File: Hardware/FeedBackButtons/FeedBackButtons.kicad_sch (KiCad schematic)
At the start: 15 parts, among them J1 Barrel_Jack_MountingPin, J2 RJ45, U1 ESP8266-01{slash}ESP-01, U2 AMS1117-3.3, U3 4N25

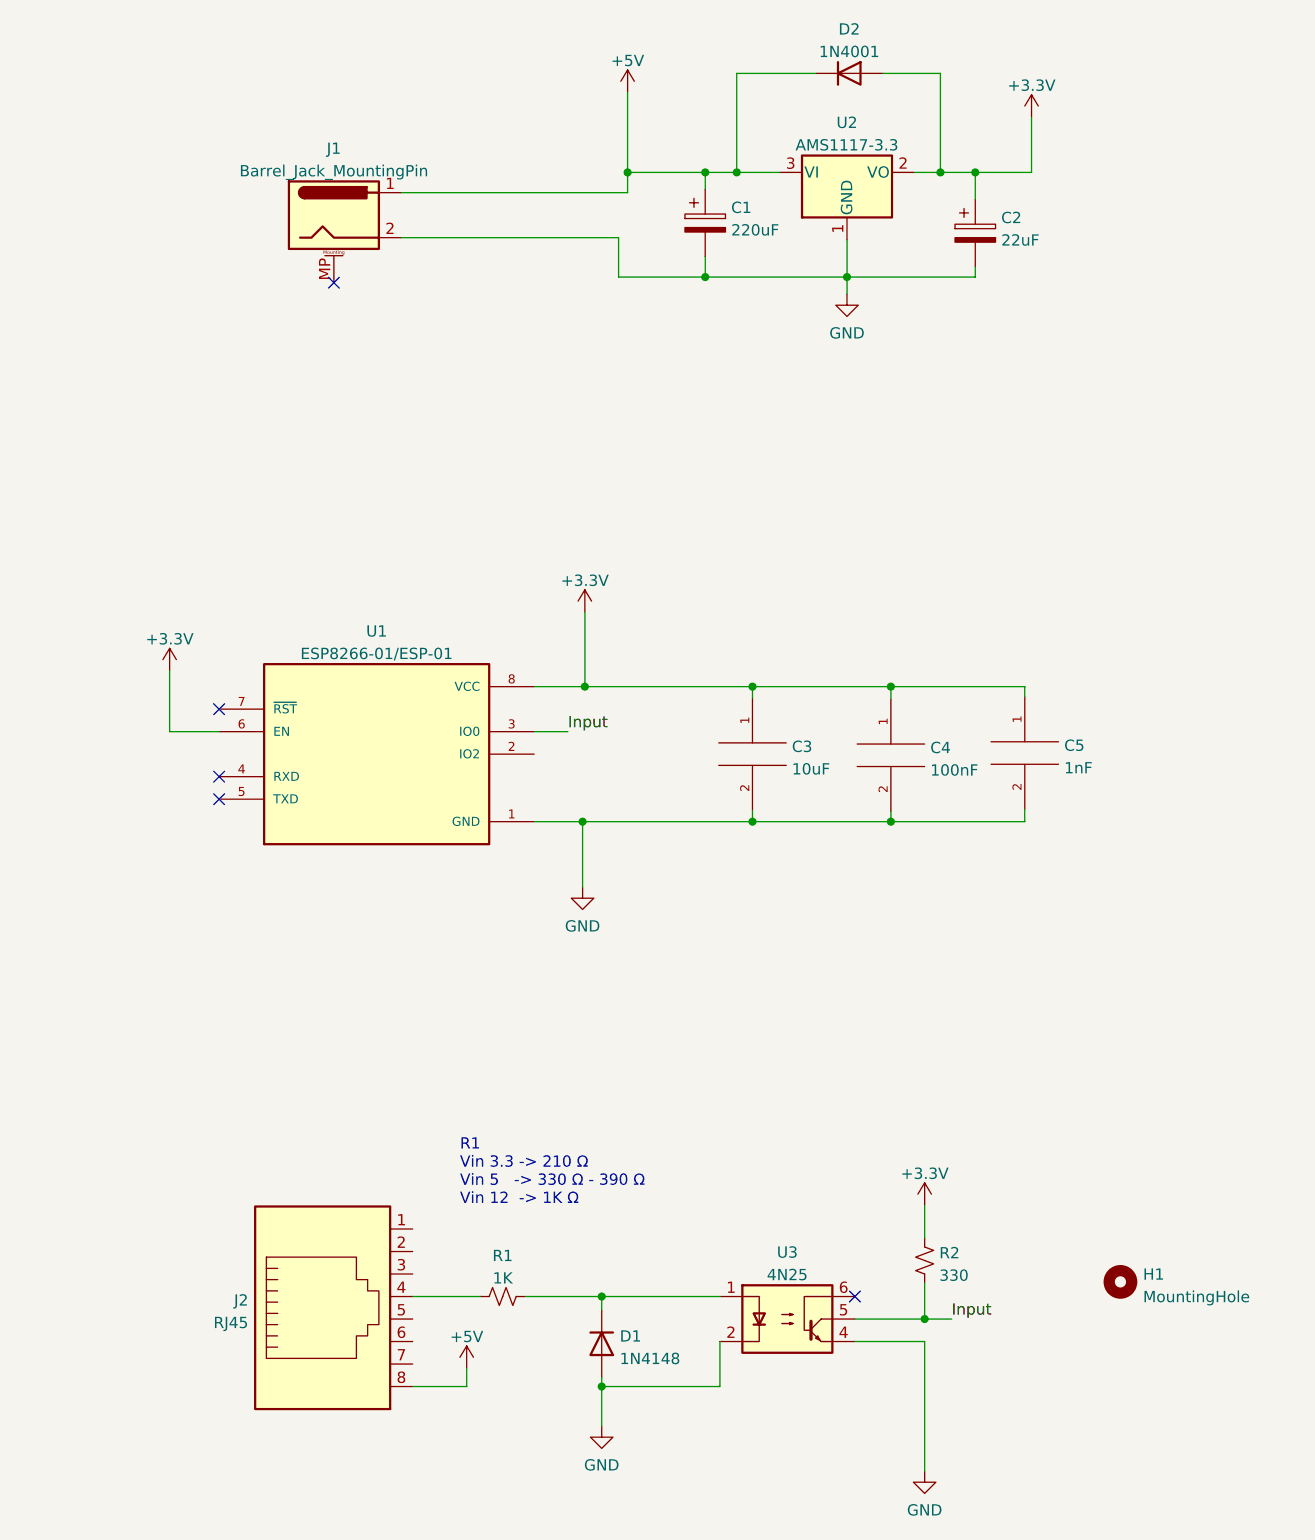
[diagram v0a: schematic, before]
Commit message: Diseño esquematico y pcb con ruteado
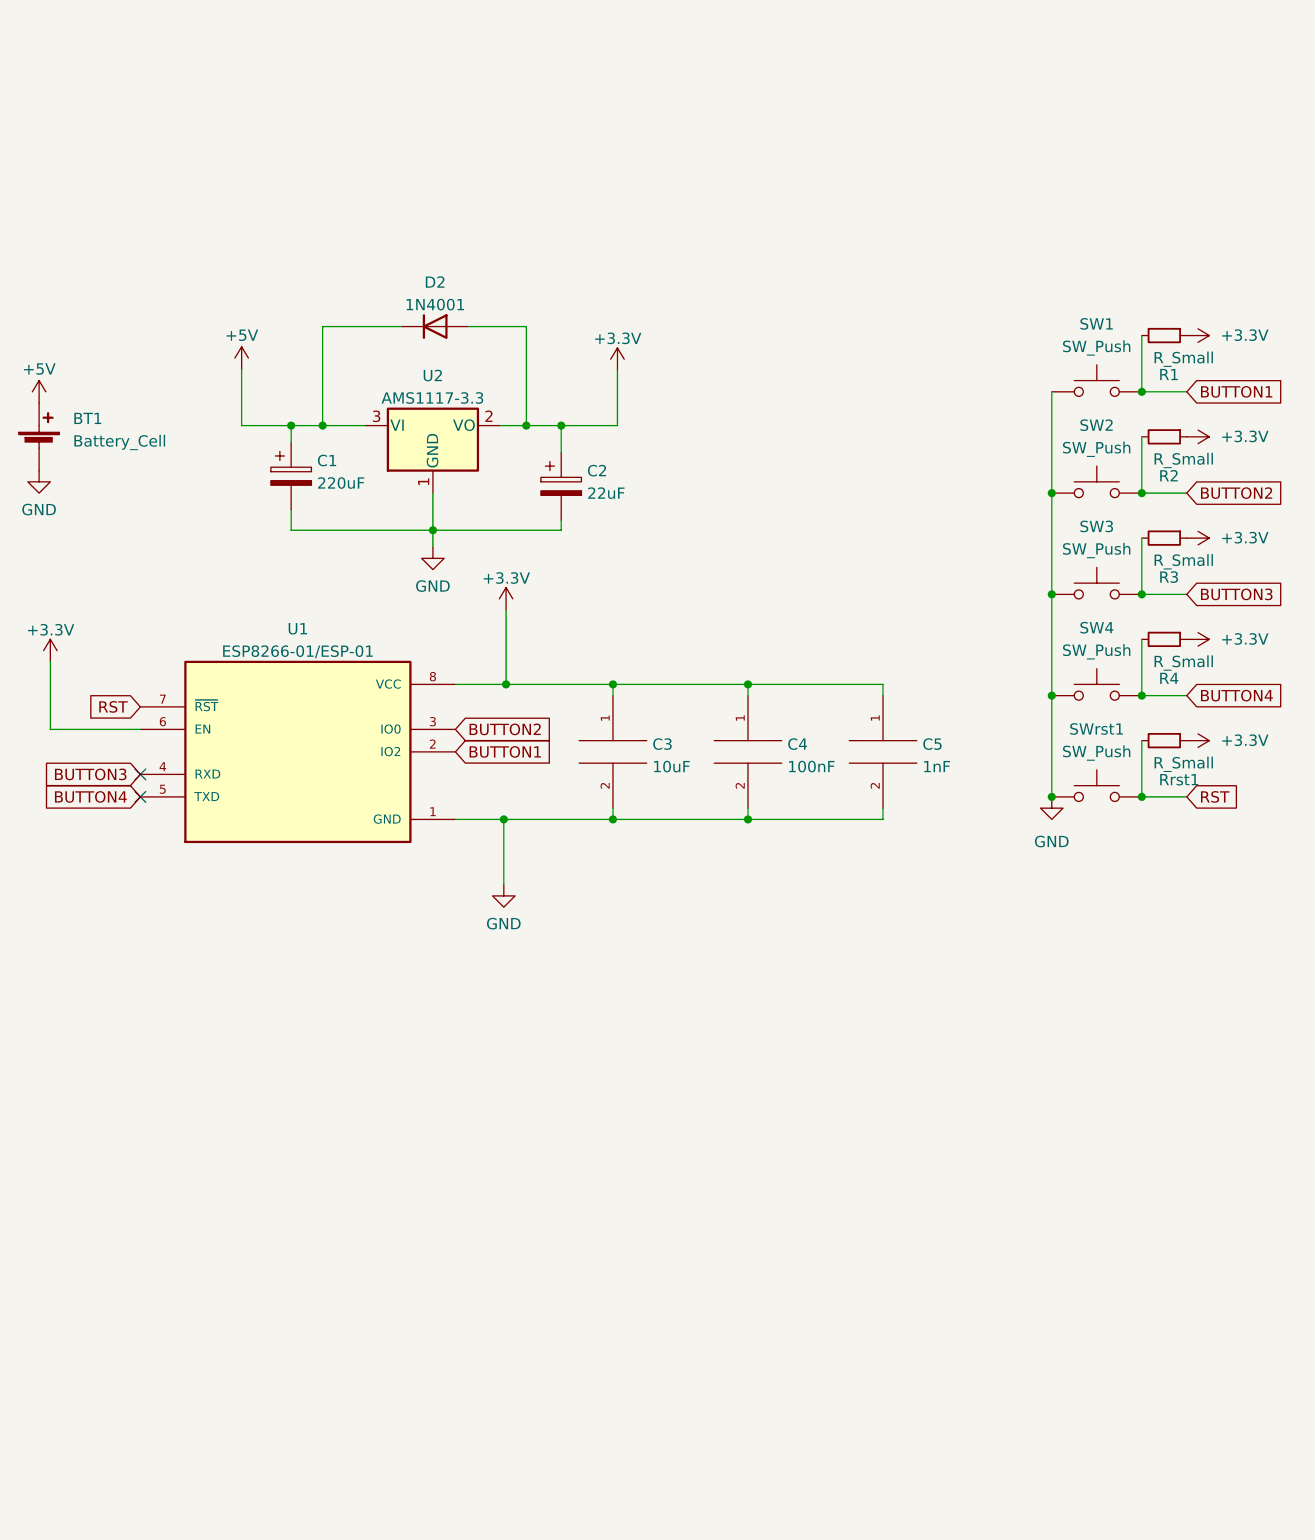
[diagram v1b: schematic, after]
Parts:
- removed D1: 1N4148, Diode_THT:D_DO-35_SOD27_P7.62mm_Horizontal, symbol Diode:1N4148
- removed H1: MountingHole, MountingHole:MountingHole_3.2mm_M3, symbol Mechanical:MountingHole
- removed J1: Barrel_Jack_MountingPin, Connector_BarrelJack:BarrelJack_GCT_DCJ200-10-A_Horizontal, symbol Connector:Barrel_Jack_MountingPin
- removed J2: RJ45, Connector_RJ:RJ45_Amphenol_54602-x08_Horizontal, symbol Connector:RJ45
- removed R1: 1K, Resistor_THT:R_Axial_DIN0309_L9.0mm_D3.2mm_P12.70mm_Horizontal, symbol Device:R_Small_US
- removed R2: 330, Resistor_THT:R_Axial_DIN0309_L9.0mm_D3.2mm_P12.70mm_Horizontal, symbol Device:R_Small_US
- removed U3: 4N25, Package_DIP:DIP-6_W7.62mm, symbol Isolator:4N25
- added BT1: Battery_Cell, Connector_PinHeader_2.54mm:PinHeader_1x02_P2.54mm_Horizontal, symbol Device:Battery_Cell
- added R1, R2, R3, R4, Rrst1: R_Small, Resistor_SMD:R_0805_2012Metric_Pad1.20x1.40mm_HandSolder, symbol Device:R_Small
- added SW1, SW2, SW3, SW4, SWrst1: SW_Push, BUTT-2:SW_BUTT-2, symbol Switch:SW_Push
- C1: footprint Capacitor_THT:CP_Radial_D7.5mm_P2.50mm -> Capacitor_SMD:C_0805_2012Metric_Pad1.18x1.45mm_HandSolder
- C2: footprint Capacitor_THT:CP_Radial_D5.0mm_P2.00mm -> Capacitor_SMD:C_0805_2012Metric_Pad1.18x1.45mm_HandSolder
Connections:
- net +3.3V: now also R1.1, R2.1, R3.1, R4.1, Rrst1.1
- net +5V: now also BT1.1 (+)
- net GND: now also BT1.2 (-), SW1.1, SW2.1, SW3.1, SW4.1, SWrst1.1
- net BUTTON1: now reaches U1.2 (IO2)
- net BUTTON1: now also R1.2, SW1.2
- net BUTTON3: now reaches U1.4 (RXD)
- net BUTTON3: now also R3.2, SW3.2
- net BUTTON4: now reaches U1.5 (TXD)
- net BUTTON4: now also R4.2, SW4.2
- net RST: now reaches U1.7 (~{RST})
- net RST: now also Rrst1.2, SWrst1.2
- net Input renamed BUTTON2
- net BUTTON2: now also R2.2, SW2.2
- no-connect marks 5 -> 2
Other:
- note removed: "R1 Vin 3.3 -> 210 Ω Vin 5 -> 330 Ω - 390 Ω Vin 12 -> 1K Ω"
- moved on the sheet: C1, C2, C3, C4, C5, D2, U1, U2
